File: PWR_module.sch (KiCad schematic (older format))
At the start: 9 parts, among them U1 VTX-214-010-205

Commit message: I have choosen a 20w 15v AC-DC converter, and have removed the rest of the converters. The power schema still has to be copied from the liteBoard.
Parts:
- removed C1, C2: 10uF, Capacitors_SMD:C_1210_HandSoldering, symbol C
- removed DC/DC_Converter1: TR05S3V3, water:TR05S3V3, symbol OKI-78SR-3.3/1.5-W36-C
- removed L1: 6.8uH, water:SRN3012TA-6R8M, symbol L
- removed SWITCH1: CONN_01X02, water:SW1811-1102-01, symbol CONN_01X02
- removed U1: VTX-214-010-205, water:VTX-214-010-205, symbol VTX-214-010-205
- added C?: 100nF, symbol C
- added L?: 10uH, symbol L
- added S?: SW_DIP_x3, symbol SW_DIP_x3
- added U?: VTX-214-020-115, symbol VTX-214-015-112
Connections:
- net labels added: +15V, 230V_GND
- net labels removed: +3.3V, +5V
- wire segments 15 -> 22
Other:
- moved on the sheet: F1
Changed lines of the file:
@@
 Comment4 ""
 $EndDescr
-Text GLabel 4100 2950 0    60   Input ~ 0
+Text GLabel 1350 1000 0    60   Input ~ 0
 230V_AC+
-Text GLabel 5900 3200 2    60   Input ~ 0
-GND
-Text GLabel 4400 3100 0    60   Input ~ 0
+Text GLabel 1350 1150 0    60   Input ~ 0
 230V_NEUTRAL
-Text GLabel 6750 3000 2    60   Input ~ 0
-+5V
-$Comp
-L OKI-78SR-3.3/1.5-W36-C DC/DC_Converter1
-U 1 1 5925452C
-P 9100 2750
-F 0 "DC/DC_Converter1" H 9300 2000 60  0000 C CNN
-F 1 "TR05S3V3" H 9100 2750 60  0000 C CNN
-F 2 "water:TR05S3V3" H 9100 2750 60  0001 C CNN
-F 3 "http://hu.farnell.com/xp-power/tr05s3v3/dc-dc-converter-0-5a-3-3v-sip/dp/2319829" H 9100 2750 60  0001 C CNN
-	1    9100 2750
-	1    0    0    -1
-$EndComp
-Text GLabel 7200 4000 0    60   Input ~ 0
-GND
-Text GLabel 7150 3350 0    60   Input ~ 0
-+5V
-Text GLabel 10100 3300 2    60   Input ~ 0
-+3.3V
-$Comp
-L CONN_01X02 SWITCH1
-U 1 1 592C9159
-P 5950 2800
-F 0 "SWITCH1" V 5950 2550 50  0000 C CNN
-F 1 "CONN_01X02" V 6050 2800 50  0000 C CNN
-F 2 "water:SW1811-1102-01" H 5950 2800 50  0001 C CNN
-F 3 "http://hu.farnell.com/marquardt/1811-1102-01/switch-spst-10a-250vac-black/dp/1839465" H 5950 2800 50  0001 C CNN
-	1    5950 2800
-	0    -1   -1   0
-$EndComp
 $Comp
 L Fuse F1
 U 1 1 592CAA69
-P 4250 2950
-F 0 "F1" V 4330 2950 50  0000 C CNN
-F 1 "Fuse" V 4175 2950 50  0000 C CNN
-F 2 "water:FUSE-0031.8201" V 4180 2950 50  0001 C CNN
-F 3 "http://hu.farnell.com/schurter/0031-8201/fuse-holder-pcb-20x5mm/dp/1162740" H 4250 2950 50  0001 C CNN
-	1    4250 2950
+P 1500 1000
+F 0 "F1" V 1580 1000 50  0000 C CNN
+F 1 "Fuse" V 1425 1000 50  0000 C CNN
+F 2 "water:FUSE-0031.8201" V 1430 1000 50  0001 C CNN
+F 3 "http://hu.farnell.com/schurter/0031-8201/fuse-holder-pcb-20x5mm/dp/1162740" H 1500 1000 50  0001 C CNN
+	1    1500 1000
 	0    1    1    0
 $EndComp
-$Comp
-L C C1
-U 1 1 593CDA13
-P 7450 3700
-F 0 "C1" H 7475 3800 50  0000 L CNN
-F 1 "10uF" H 7475 3600 50  0000 L CNN
-F 2 "Capacitors_SMD:C_1210_HandSoldering" H 7488 3550 50  0001 C CNN
-F 3 "http://hu.farnell.com/vishay/vj1206y106kxxtw1bc/cap-mlcc-x7r-10uf-25v-1206/dp/2407348" H 7450 3700 50  0001 C CNN
-	1    7450 3700
-	1    0    0    -1
-$EndComp
-$Comp
-L C C2
-U 1 1 593CDA6C
-P 7950 3700
-F 0 "C2" H 7975 3800 50  0000 L CNN
-F 1 "10uF" H 7975 3600 50  0000 L CNN
-F 2 "Capacitors_SMD:C_1210_HandSoldering" H 7988 3550 50  0001 C CNN
-F 3 "http://hu.farnell.com/vishay/vj1206y106kxxtw1bc/cap-mlcc-x7r-10uf-25v-1206/dp/2407348" H 7950 3700 50  0001 C CNN
-	1    7950 3700
-	1    0    0    -1
-$EndComp
-$Comp
-L L L1
-U 1 1 593CDA97
-P 7700 3350
-F 0 "L1" V 7650 3350 50  0000 C CNN
-F 1 "6.8uH" V 7775 3350 50  0000 C CNN
-F 2 "water:SRN3012TA-6R8M" H 7700 3350 50  0001 C CNN
-F 3 "http://hu.farnell.com/bourns/srn3012ta-6r8m/inductor-aec-q200-6-8uh-1-05a/dp/2616860" H 7700 3350 50  0001 C CNN
-	1    7700 3350
-	0    1    1    0
-$EndComp
-Wire Wire Line
-	7150 3350 7550 3350
-Wire Wire Line
-	7450 3550 7450 3350
-Connection ~ 7450 3350
-Wire Wire Line
-	7850 3350 8350 3350
-Wire Wire Line
-	8350 3350 8350 2950
-Wire Wire Line
-	8350 2950 8800 2950
-Wire Wire Line
-	7200 4000 8550 4000
-Wire Wire Line
-	8550 4000 8550 3100
-Wire Wire Line
-	8550 3100 8800 3100
-Wire Wire Line
-	7950 3550 7950 3350
-Connection ~ 7950 3350
-Wire Wire Line
-	7950 3850 7950 4000
-Connection ~ 7950 4000
-Wire Wire Line
-	7450 3850 7450 4000
-Connection ~ 7450 4000
 $Comp
 L R R26
@@
 Wire Wire Line
 	6500 3000 6500 2800
-Wire Wire Line
-	6000 3000 6750 3000
 Connection ~ 6500 3000
 $Comp
-L VTX-214-010-205 U1
-U 1 1 593CF1AF
-P 5200 2650
-F 0 "U1" H 5150 1800 60  0000 C CNN
-F 1 "VTX-214-010-205" H 5200 2650 60  0000 C CNN
-F 2 "water:VTX-214-010-205" H 5200 2650 60  0001 C CNN
-F 3 "http://hu.farnell.com/vigortronix/vtx-214-010-205/power-supply-ac-dc-5v-2a/dp/2464685" H 5200 2650 60  0001 C CNN
-	1    5200 2650
+L VTX-214-015-112 U?
+U 1 1 59A46413
+P 3450 700
+F 0 "U?" H 3400 -150 60  0000 C CNN
+F 1 "VTX-214-020-115" H 3450 700 60  0000 C CNN
+F 2 "" H 3450 700 60  0001 C CNN
+F 3 "http://hu.farnell.com/vigortronix/vtx-214-020-115/power-supply-ac-dc-15v-1-333a/dp/2464706" H 3450 700 60  0001 C CNN
+	1    3450 700
 	1    0    0    -1
 $EndComp
+Text GLabel 1350 1300 0    60   Input ~ 0
+230V_GND
+Text GLabel 5100 1250 2    60   Input ~ 0
+GND
+Text GLabel 5100 950  2    60   Input ~ 0
++15V
+$Comp
+L C C?
+U 1 1 59A480E8
+P 4800 1100
+F 0 "C?" H 4825 1200 50  0000 L CNN
+F 1 "100nF" H 4825 1000 50  0000 L CNN
+F 2 "" H 4838 950 50  0001 C CNN
+F 3 "" H 4800 1100 50  0001 C CNN
+	1    4800 1100
+	1    0    0    -1
+$EndComp
+$Comp
+L L L?
+U 1 1 59A481DD
+P 4450 950
+F 0 "L?" V 4400 950 50  0000 C CNN
+F 1 "10uH" V 4525 950 50  0000 C CNN
+F 2 "" H 4450 950 50  0001 C CNN
+F 3 "http://hu.farnell.com/laird-technologies/tys5040100m-10/inductor-10-h-smd/dp/2292532" H 4450 950 50  0001 C CNN
+F 4 "http://hu.farnell.com/bourns/srn5040-100m/inductor-semi-shld-10uh-20-2-1a/dp/2428234" V 4450 950 60  0001 C CNN "semishielded"
+	1    4450 950
+	0    1    1    0
+$EndComp
+Connection ~ 4800 1250
+Wire Wire Line
+	4150 1050 4250 1050
+Wire Wire Line
+	4250 1050 4250 950
+Wire Wire Line
+	4600 950  5100 950
+Connection ~ 4800 950
+Wire Wire Line
+	4250 950  4300 950
+Wire Wire Line
+	5100 1250 4150 1250
+Wire Wire Line
+	1650 1000 1750 1000
+$Comp
+L SW_DIP_x3 S?
+U 1 1 59A4BDAD
+P 2150 1150
+F 0 "S?" H 2150 950 50  0000 C CNN
+F 1 "SW_DIP_x3" H 2150 1350 50  0000 C CNN
+F 2 "" H 2100 1150 60  0000 C CNN
+F 3 "" H 2100 1150 60  0000 C CNN
+	1    2150 1150
+	1    0    0    -1
+$EndComp
+Wire Wire Line
+	2450 1150 2650 1150
+Wire Wire Line
+	2450 1250 2550 1250
+Wire Wire Line
+	2550 1250 2550 1300
+Wire Wire Line
+	2550 1300 2650 1300
+Wire Wire Line
+	2450 1050 2550 1050
+Wire Wire Line
+	2550 1050 2550 1000
+Wire Wire Line
+	2550 1000 2650 1000
+Wire Wire Line
+	1350 1150 1850 1150
+Wire Wire Line
+	1350 1300 1750 1300
+Wire Wire Line
+	1750 1300 1750 1250
+Wire Wire Line
+	1750 1250 1850 1250
+Wire Wire Line
+	1750 1000 1750 1050
+Wire Wire Line
+	1750 1050 1850 1050
 $EndSCHEMATC

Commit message: feature complete; the next step is the verification of the values and the schematics
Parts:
- added C? (x4): 10uF, symbol C
- added C? (x2): 0.1uF, symbol C
- added C? (x2): 2.2nF, symbol C
- added C? (x4): 22uF, symbol C
- added C? (x2): C_P, symbol C
- added C? (x2): 0.1uF, symbol C_Small
- added C?: C, symbol C
- added C?: 47uF, symbol C
- added C?: 100nF, symbol C
- added D?: D_TVS_ALT, symbol D_TVS_ALT
- added L?: 3.6uH, symbol L
- added L?: 10uH, symbol L
- added L?: 6.8uH, symbol L
- added Q?: BS250, TO_SOT_Packages_THT:TO-92_Molded_Narrow, symbol BS250
- added R? (x2): 100k, symbol R
- added R?: 22k, symbol R
- added R?: 75k, symbol R_Small
- added R?: 24k, symbol R_Small
- added R?: 33k, symbol R
- added R?: 62k 0.1%, symbol R_Small
- added R?: 11k8 0.1%, symbol R_Small
- added U? (x2): RT7297BHZSP, symbol RT7297BHZSP
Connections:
- net labels added: +3.3V, +5V, P1
- wire segments 22 -> 93
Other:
- note added: "3.3V Output after the Step-Down \nRegulator"
- note added: "5V Output after the Step-Down \nRegulator"
- note added: "Power LED"
- moved on the sheet: D15, R26

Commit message: this version contains the datasheets and the footprints of the parts
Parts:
- removed C? (x2): 100nF, symbol C
- removed C? (x4): 10uF, symbol C
- removed C? (x2): 0.1uF, symbol C
- removed C? (x2): 0.1uF, symbol C_Small
- removed C? (x3): 22uF, symbol C
- removed C?: C, symbol C
- removed C?: 2.2nF, symbol C
- removed L?: 10uH, symbol L
- removed R26: 330, Resistors_SMD:R_1206_HandSoldering, symbol R
- removed R? (x2): 100k, symbol R
- added C?: X2: 0.22uF, Capacitors_THT:C_Rect_L18.0mm_W8.0mm_P15.00mm_FKS3_FKP3, symbol C
- added C? (x6): 100nF, Capacitors_SMD:C_0603_HandSoldering, symbol C
- added C? (x4): 10uF, Capacitors_SMD:C_0603_HandSoldering, symbol C
- added C?: 2.2nF, Resistors_SMD:R_0603_HandSoldering, symbol C
- added C? (x3): 22uF, Capacitors_SMD:C_0603_HandSoldering, symbol C
- added FL?: BU9S-153R15BL, water:BU9S-153R15BL, symbol EMI_Filter_CommonMode
- added J? (x3): CONN_01X01, Connectors:PINTST, symbol CONN_01X01
- added R?: 10kΩ, Resistors_SMD:R_0603_HandSoldering, symbol R
- added R?: 100k, Resistors_SMD:R_0603_HandSoldering, symbol R
- added R?: 2kΩ, Resistors_SMD:R_0603_HandSoldering, symbol R
- added RV?: 14D431KTR, Varistors:RV_Disc_D21.5_W5.3_P10, symbol Varistor
- C?, R? (x3): footprint (none) -> Resistors_SMD:R_0603_HandSoldering
- C?: footprint (none) -> Capacitors_SMD:C_0603_HandSoldering
- C?: footprint (none) -> Capacitors_SMD:C_1206_HandSoldering
- L? (x2): footprint (none) -> inductor:SM-INDUCTOR_12.5mmX12.5mm
- L?: value 10uH -> 300@100M; footprint (none) -> Inductors_SMD:L_0603_HandSoldering; semishielded http://hu.farnell.com/bourns/srn5040-100m/inductor-semi-shl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 -> (none)
- R?: value 75k -> 75k 0.1%; footprint (none) -> Resistors_SMD:R_0603_HandSoldering
- R?: value 24k -> 24k 0.1%; footprint (none) -> Resistors_SMD:R_0603_HandSoldering
- R?: footprint (none) -> http://hu.farnell.com/te-connectivity/cpf0603b11k8e1/res-thin-film-11k8-0-1-0-063w/dp/2330890
- U?: footprint (none) -> water:VTX-214-015-112
- U? (x2): footprint (none) -> sop:SOP8_ep
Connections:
- net labels added: PMIC_ON_REQ
- wire segments 93 -> 104
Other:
- moved on the sheet: C?, D15, U?

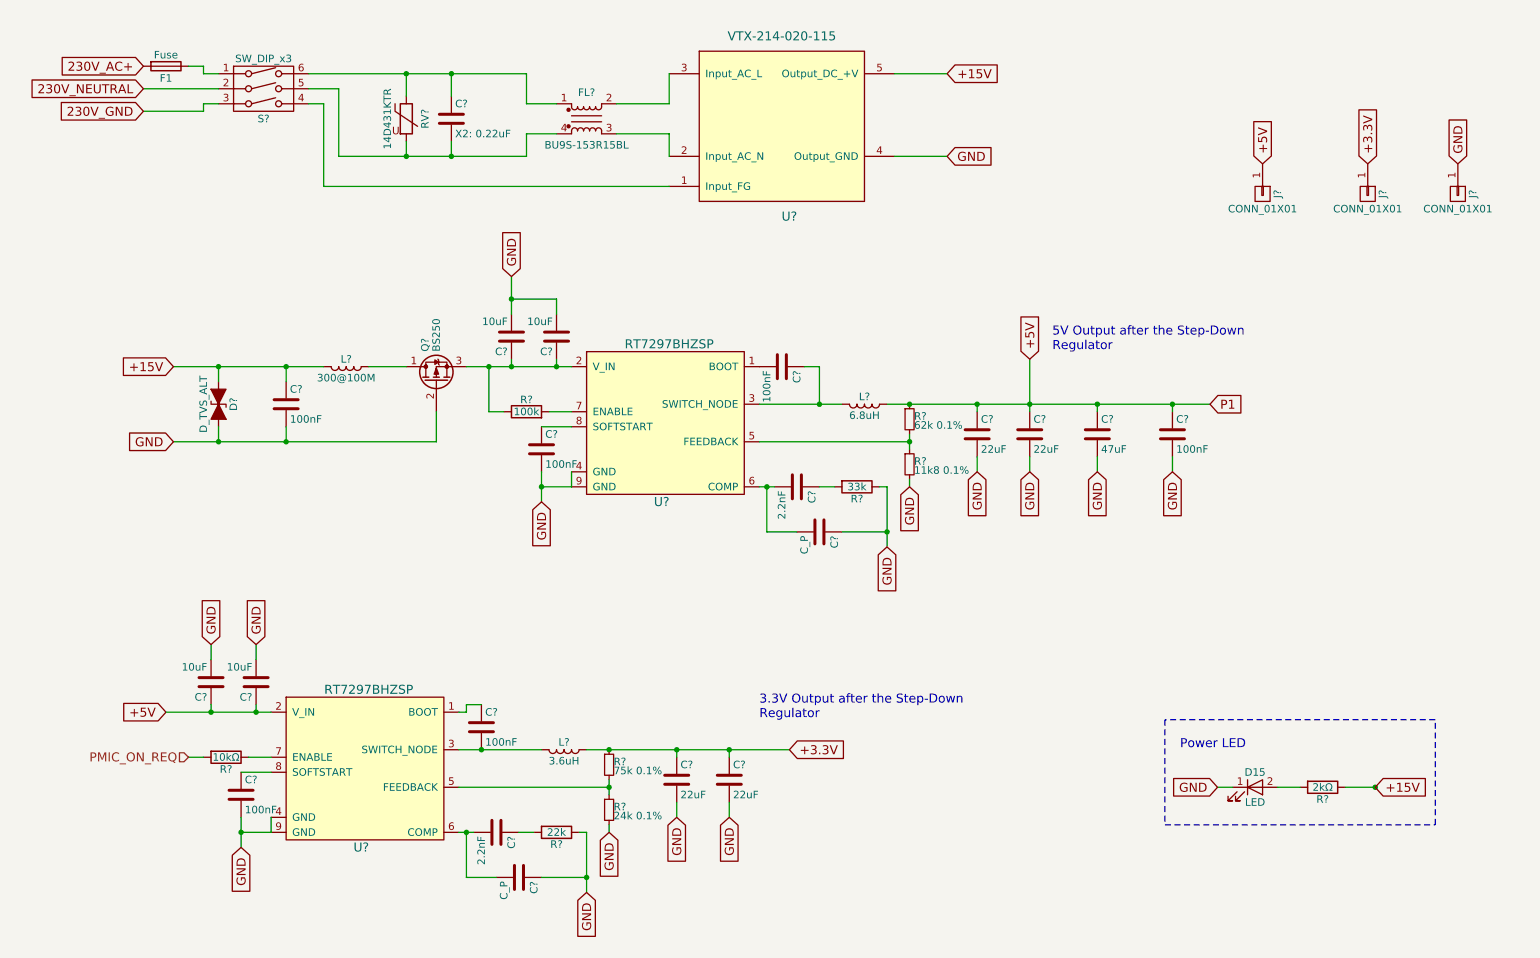
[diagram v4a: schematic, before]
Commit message: some issues fixed by the bugfixer; formal verification needed
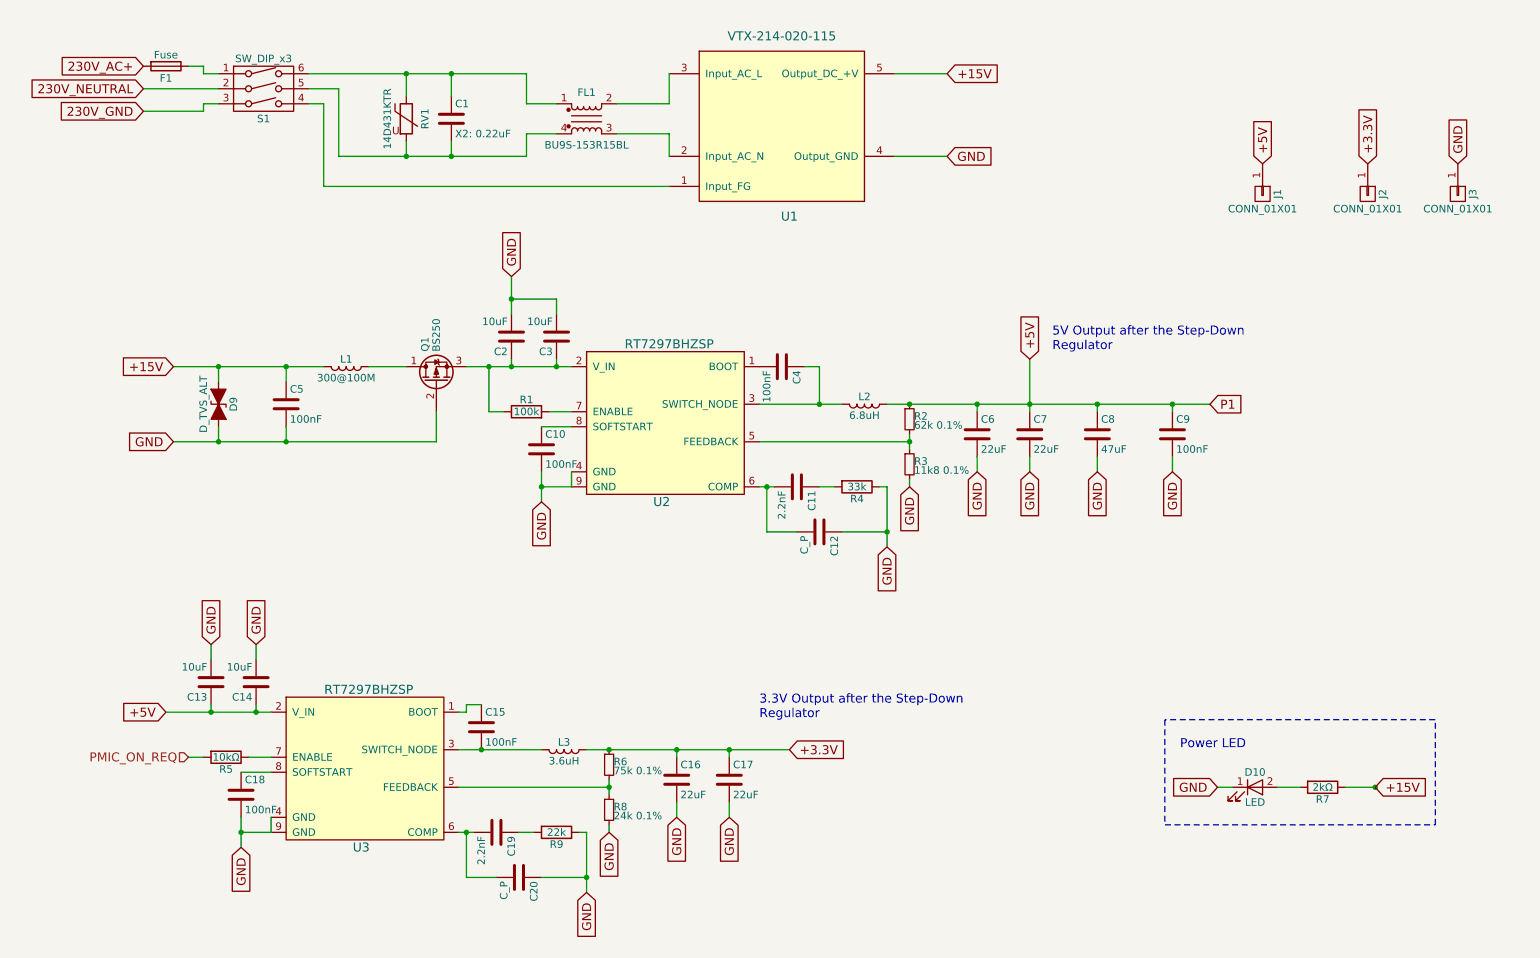
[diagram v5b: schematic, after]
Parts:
- gave numbers to parts that had none: 43
- renumbered D15 to D10
